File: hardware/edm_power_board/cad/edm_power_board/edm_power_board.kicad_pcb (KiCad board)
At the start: 2 copper layers, 240 x 100 mm, 147 parts, among them J501 Conn_02x08_Odd_Even, J502 Conn_01x02, Q201 SUD19P06-60, Q301 BSS214NW, Q302 BSC13DN30NSFD, Q303 BSS214NW, Q304 BSS214NW, Q601 IPD50R3K0CE, Q602 IPD50R380CE, U201 LM358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

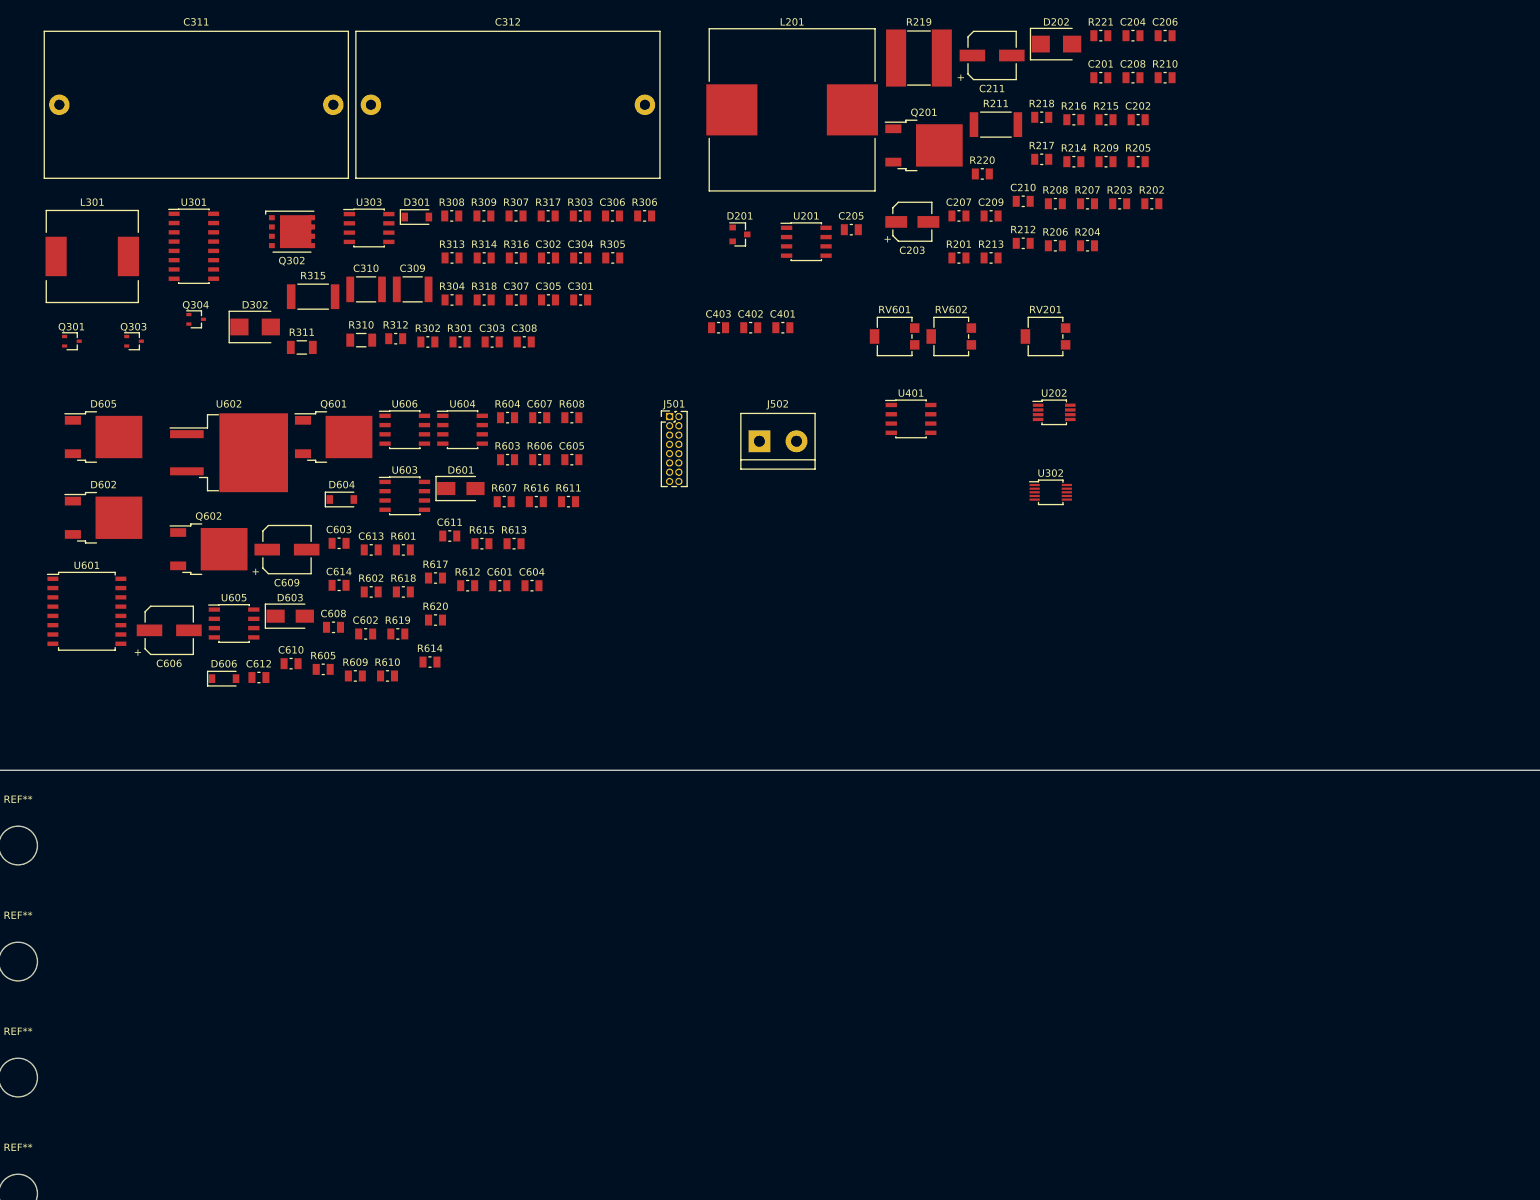
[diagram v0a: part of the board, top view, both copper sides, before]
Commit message: Add input capacitors to spark
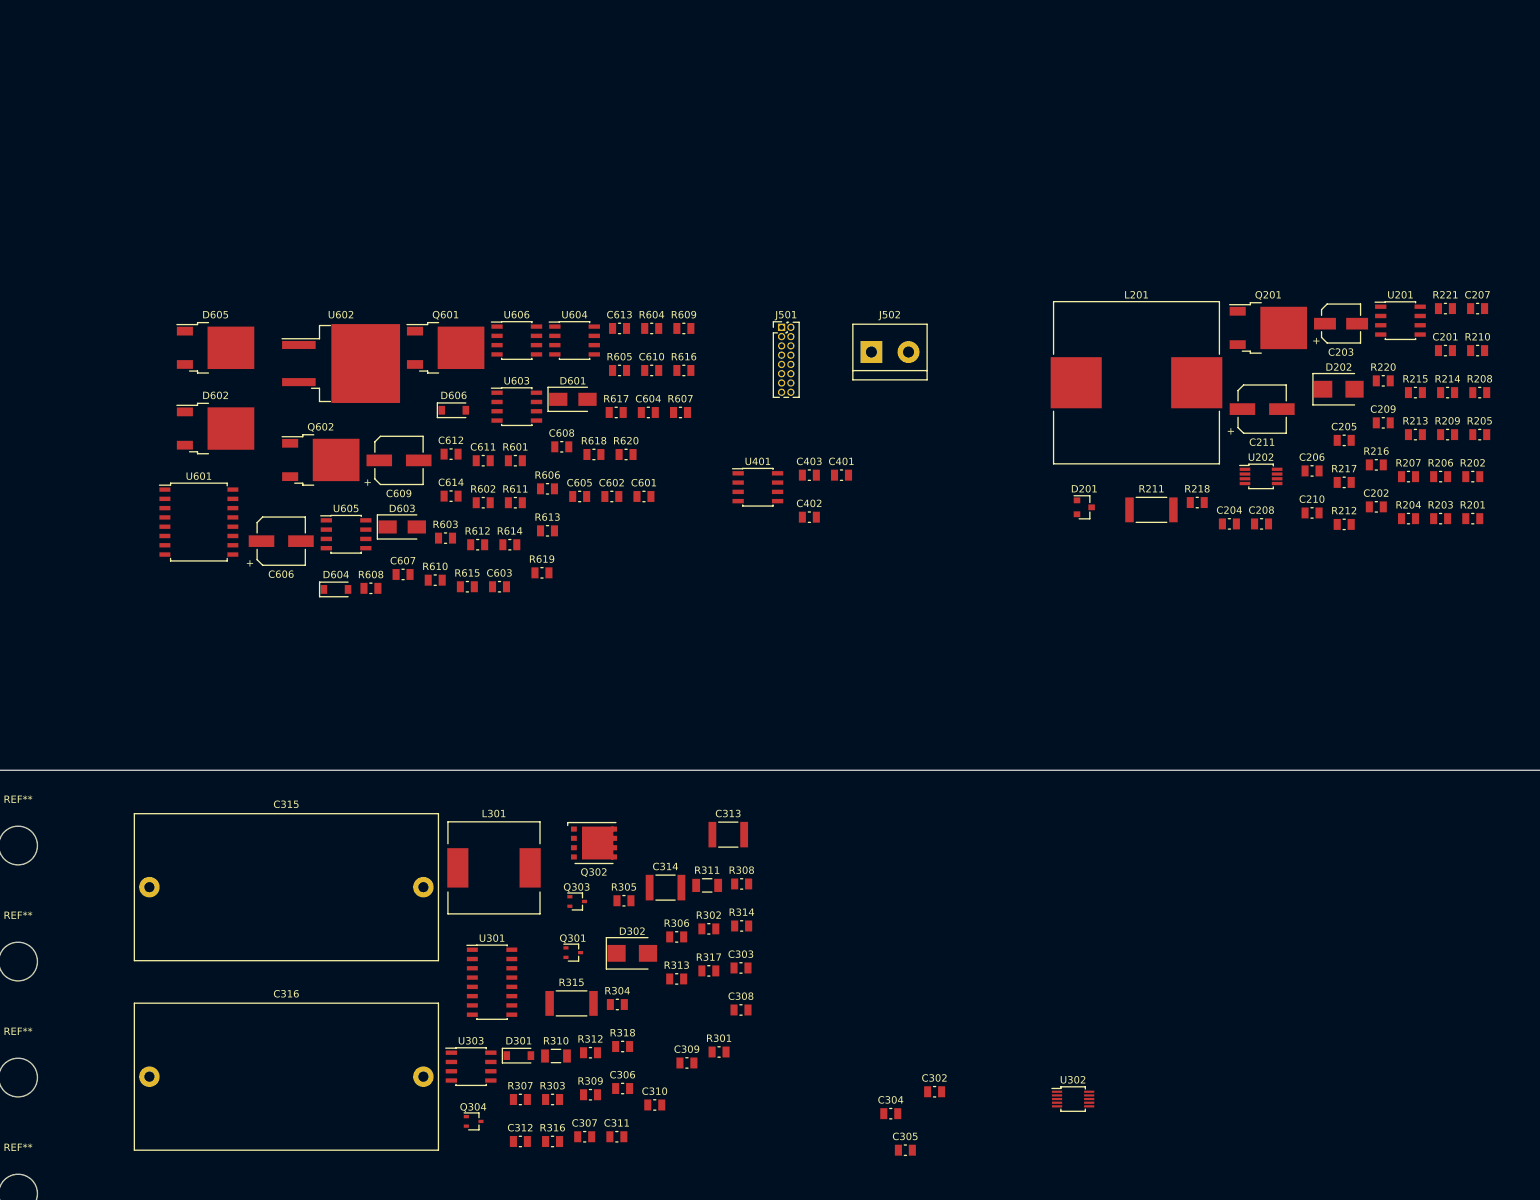
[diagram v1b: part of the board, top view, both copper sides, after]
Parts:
- removed C301: 100n, Capacitor_SMD:C_0805_2012Metric
- removed R219: 20m, Resistor_SMD:R_Stackpole_CSSH2728_4-100m
- removed RV201, RV601: 50k, Potentiometer_SMD:Potentiometer_Bourns_3314G_Horizontal
- removed RV602: 250k, Potentiometer_SMD:Potentiometer_Bourns_3314G_Horizontal
- added C313: 470n, Capacitor_SMD:C_1812_4532Metric, F.Cu at (102.8, -91.2)
- added C314: 470n, Capacitor_SMD:C_1812_4532Metric, F.Cu at (94.2, -83.9)
- added C315: 25u, Capacitor_THT:C_Rect_L41.5mm_W20.0mm_P37.50mm_MKS4, F.Cu at (23.6, -84.0)
- added C316: 25u, Capacitor_THT:C_Rect_L41.5mm_W20.0mm_P37.50mm_MKS4, F.Cu at (23.6, -58.1)
- C302: value 10n -> 1u
- C304: value 100n -> 1u
- C306: value 120n -> 10n
- C307: value 560p -> 100n
- C308: value 1n -> 100n
- C309: value 470n -> 1u; footprint Capacitor_SMD:C_1812_4532Metric -> Capacitor_SMD:C_0805_2012Metric
- C310: value 470n -> 120n; footprint Capacitor_SMD:C_1812_4532Metric -> Capacitor_SMD:C_0805_2012Metric
- C311: value 25u -> 560p; footprint Capacitor_THT:C_Rect_L41.5mm_W20.0mm_P37.50mm_MKS4 -> Capacitor_SMD:C_0805_2012Metric
- C312: value 25u -> 1n; footprint Capacitor_THT:C_Rect_L41.5mm_W20.0mm_P37.50mm_MKS4 -> Capacitor_SMD:C_0805_2012Metric
- moved C311 160.5 mm to (87.6, -49.8)
- moved C312 143.4 mm to (74.4, -49.2)
- moved C305 126.2 mm to (127.0, -48.0)
- moved C302 125.8 mm to (131.0, -56.0)
- moved C304 124.6 mm to (125.0, -53.0)
- moved R309 121.2 mm to (83.9, -55.6)
- moved R316 121.0 mm to (78.8, -49.2)
- moved R303 121.0 mm to (78.8, -54.9)
- moved R307 120.9 mm to (74.4, -54.9)
- moved C306 119.4 mm to (88.3, -56.4)
- moved C310 118.4 mm to (92.7, -54.2)
- moved Q304 116.2 mm to (68.0, -51.9)
- moved D301 115.6 mm to (74.1, -60.9)
- moved U303 115.6 mm to (67.6, -59.4)
- moved C307 114.9 mm to (83.2, -49.8)
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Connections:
- C302 pad 1: Net-(C302-Pad1) -> +24V
- C303 pad 1: +5V -> +3V3
- C303 pad 2: GNDPWR -> GND
- C304 pad 1: +5V -> +24V
- C305 pad 1: Net-(C305-Pad1) -> +24V
- C306 pad 2: Net-(C306-Pad2) -> GNDPWR
- C307 pad 1: Net-(C306-Pad1) -> +5V
- C307 pad 2: Net-(C307-Pad2) -> GNDPWR
- C308 pad 1: Net-(C308-Pad1) -> +5V
- C309 pad 1: /Spark Output/+250V -> Net-(C309-Pad1)
- C310 pad 1: /Spark Output/+250V -> Net-(C310-Pad1)
- C310 pad 2: GNDPWR -> Net-(C310-Pad2)
- C311 pad 1: /Spark Output/+250V -> Net-(C310-Pad1)
- C311 pad 2: GNDPWR -> Net-(C311-Pad2)
- C312 pad 1: /Spark Output/+250V -> Net-(C312-Pad1)
- R305 pad 1: Net-(C306-Pad2) -> Net-(C310-Pad2)
- R305 pad 2: Net-(C307-Pad2) -> Net-(C311-Pad2)
- R308 pad 1: Net-(C306-Pad1) -> Net-(C310-Pad1)
- R309 pad 1: Net-(C308-Pad1) -> Net-(C312-Pad1)
- R313 pad 1: Net-(C306-Pad1) -> Net-(C310-Pad1)
- R314 pad 2: Net-(C308-Pad1) -> Net-(C312-Pad1)
- R316 pad 1: Net-(C306-Pad1) -> Net-(C310-Pad1)
- R317 pad 2: Net-(C306-Pad1) -> Net-(C310-Pad1)
- R318 pad 1: Net-(C306-Pad1) -> Net-(C310-Pad1)
- U302 pad 10: Net-(C302-Pad1) -> Net-(C306-Pad1)
- U302 pad 2: Net-(C306-Pad1) -> Net-(C310-Pad1)
- U302 pad 3: Net-(C307-Pad2) -> Net-(C311-Pad2)
- U302 pad 4: Net-(C305-Pad1) -> Net-(C309-Pad1)

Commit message: Component placement 250V
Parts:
- added C301: 22u, Capacitor_SMD:CP_Elec_5x5.3, F.Cu at (125.2, -42.1)
- added R219: 20m, Resistor_SMD:R_Stackpole_CSSH2728_4-100m, F.Cu at (216.2, -139.1)
- added RV201: 50k, Potentiometer_SMD:Potentiometer_Bourns_3314G_Horizontal, F.Cu at (10.2, -151.8)
- added RV601: 50k, Potentiometer_SMD:Potentiometer_Bourns_3314G_Horizontal, F.Cu at (-10.4, -151.8)
- added RV602: 250k, Potentiometer_SMD:Potentiometer_Bourns_3314G_Horizontal, F.Cu at (-2.67, -151.8)
- moved C316 147.9 mm to (169.6, -81.5)
- moved J501 140.9 mm to (221.1, -73.9)
- moved U301 108.4 mm to (169.2, -26.2), turned to 180 degrees
- moved C315 102.5 mm to (126.0, -81.4)
- moved Q304 96.0 mm to (159.2, -22.2), turned to 180 degrees
- moved Q303 96.0 mm to (159.2, -24.9), turned to 180 degrees
- moved U303 94.5 mm to (160.4, -41.6)
- moved Q301 91.0 mm to (159.2, -27.6), turned to 180 degrees
- moved D301 88.2 mm to (158.7, -35.6)
- moved R304 83.1 mm to (166.0, -40.2), turned to 270 degrees
- moved C307 83.1 mm to (166.0, -43.9), turned to 90 degrees
- moved R310 81.4 mm to (154.8, -30.6)
- moved R308 80.7 mm to (155.6, -21.9)
- moved L301 80.7 mm to (128.6, -30.4), turned to 270 degrees
- moved R307 80.5 mm to (153.5, -40.3), turned to 270 degrees
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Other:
- copper layers 2 -> 4

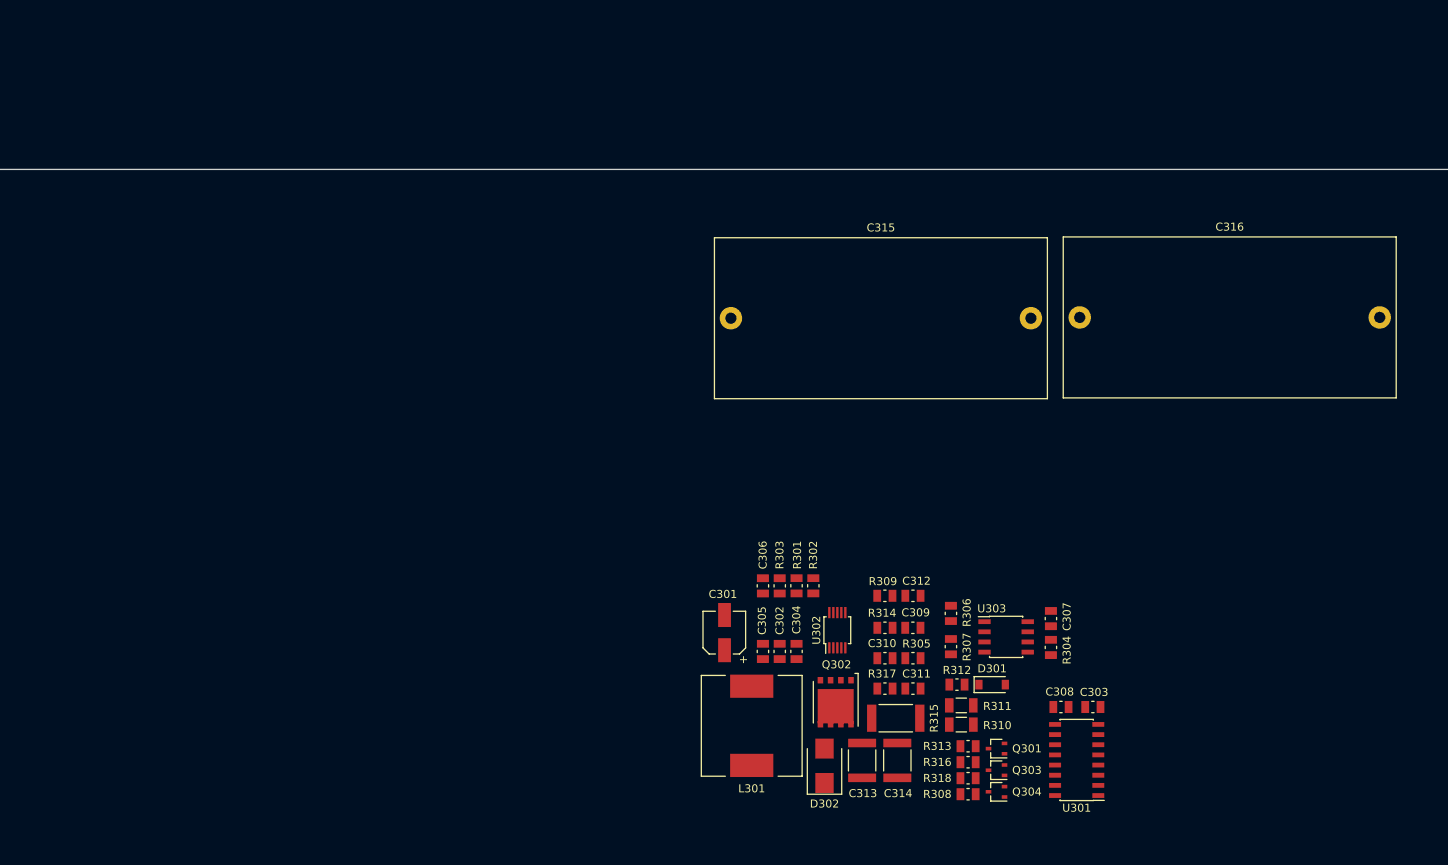
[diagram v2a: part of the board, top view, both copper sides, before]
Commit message: Spark output connector
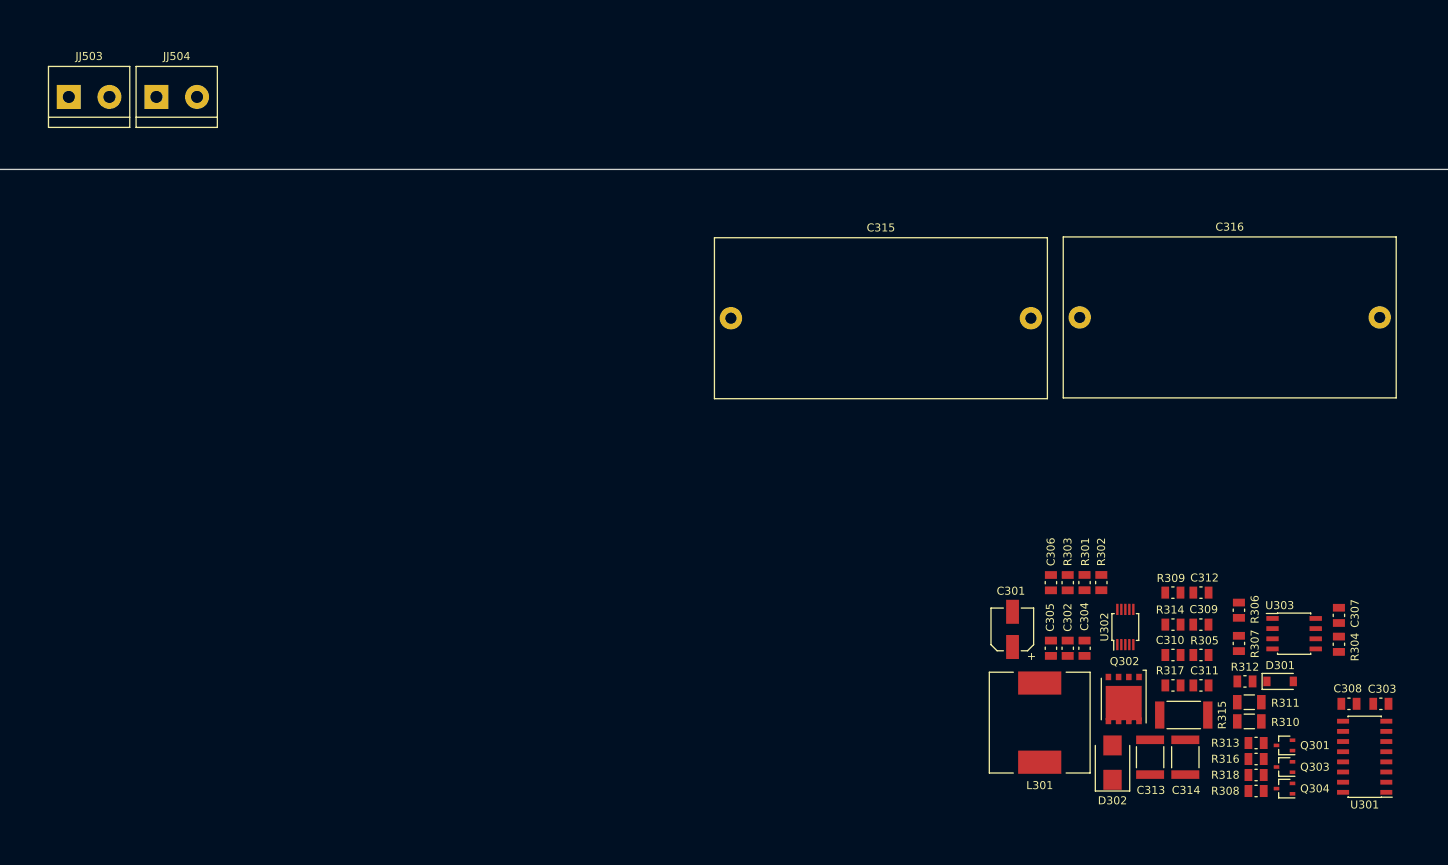
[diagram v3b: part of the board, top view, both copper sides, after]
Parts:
- added JJ503: Conn_01x02, TerminalBlock:TerminalBlock_bornier-2_P5.08mm, F.Cu at (43.2, -109.1)
- added JJ504: Conn_01x02, TerminalBlock:TerminalBlock_bornier-2_P5.08mm, F.Cu at (54.2, -109.1)
- moved C302 36.0 mm to (168.1, -40.1)
- moved C303 36.0 mm to (207.2, -33.2)
- moved C304 36.0 mm to (170.2, -40.1)
- moved C305 36.0 mm to (166.0, -40.1)
- moved C306 36.0 mm to (166.0, -48.3)
- moved C307 36.0 mm to (202.0, -44.3)
- moved C308 36.0 mm to (203.3, -33.2)
- moved C309 36.0 mm to (184.7, -43.1)
- moved C310 36.0 mm to (181.3, -39.3)
- moved C311 36.0 mm to (184.8, -35.5)
- moved C312 36.0 mm to (184.8, -47.1)
- moved C313 36.0 mm to (178.4, -26.5)
- moved C314 36.0 mm to (182.8, -26.5)
- moved D301 36.0 mm to (194.7, -36.0)
- moved D302 36.0 mm to (173.7, -25.9)
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
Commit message: Plated mounting holes
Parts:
- removed REF** (x12): MountingHole_5.3mm_M5, MountingHole:MountingHole_5.3mm_M5
- added MK501: Mounting_Hole_PAD, MountingHole:MountingHole_5mm_Pad, F.Cu at (5.60, -10.3)
- added MK502: Mounting_Hole_PAD, MountingHole:MountingHole_5mm_Pad, F.Cu at (5.60, -26.2)
- added MK503: Mounting_Hole_PAD, MountingHole:MountingHole_5mm_Pad, F.Cu at (5.60, -42.1)
- added MK504: Mounting_Hole_PAD, MountingHole:MountingHole_5mm_Pad, F.Cu at (5.60, -57.9)
- added MK505: Mounting_Hole_PAD, MountingHole:MountingHole_5mm_Pad, F.Cu at (5.60, -73.8)
- added MK506: Mounting_Hole_PAD, MountingHole:MountingHole_5mm_Pad, F.Cu at (5.60, -89.7)
- added MK507: Mounting_Hole_PAD, MountingHole:MountingHole_5mm_Pad, F.Cu at (234.4, -10.3)
- added MK508: Mounting_Hole_PAD, MountingHole:MountingHole_5mm_Pad, F.Cu at (234.4, -26.2)
- added MK509: Mounting_Hole_PAD, MountingHole:MountingHole_5mm_Pad, F.Cu at (234.4, -42.1)
- added MK510: Mounting_Hole_PAD, MountingHole:MountingHole_5mm_Pad, F.Cu at (234.4, -57.9)
- added MK511: Mounting_Hole_PAD, MountingHole:MountingHole_5mm_Pad, F.Cu at (234.4, -73.8)
- added MK512: Mounting_Hole_PAD, MountingHole:MountingHole_5mm_Pad, F.Cu at (234.4, -89.7)
- U301: value Si8641BB-B-IS1 -> Si8641BB-B-IS; footprint Package_SO:SOIC-16_3.9x9.9mm_P1.27mm -> Package_SO:SOIC-16W_7.5x10.3mm_P1.27mm
- moved R214 180.0 mm to (58.5, -42.1), turned to 270 degrees
- moved C207 178.7 mm to (69.3, -47.4), turned to 270 degrees
- moved R210 178.3 mm to (65.1, -47.4), turned to 270 degrees
- moved C209 172.2 mm to (56.4, -42.0), turned to 90 degrees
- moved R213 171.3 mm to (60.6, -42.1), turned to 90 degrees
- moved D202 171.3 mm to (71.3, -25.2)
- moved R209 171.3 mm to (68.7, -37.4), turned to 90 degrees
- moved R205 170.0 mm to (67.2, -47.4), turned to 270 degrees
- moved C211 165.7 mm to (47.2, -45.1), turned to 90 degrees
- moved Q201 165.5 mm to (73.2, -31.4)
- moved L201 162.8 mm to (55.6, -27.1), turned to 90 degrees
- moved C203 161.6 mm to (75.6, -43.7), turned to 90 degrees
- moved R212 161.3 mm to (54.3, -42.0), turned to 270 degrees
- moved C210 160.4 mm to (52.2, -42.0), turned to 90 degrees
- moved U202 147.3 mm to (65.8, -42.1)
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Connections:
- net Net-(C201-Pad1) renamed /Current Source/CS_2-
- net Net-(C205-Pad1) renamed /Current Source/CS_1
- net Net-(C205-Pad2) renamed /Current Source/CS_2+
- net Net-(C206-Pad1) renamed /Current Source/CS_3
- net Net-(C206-Pad2) renamed /Current Source/CS_2
- net Net-(C207-Pad2) renamed /Current Source/CS_VCC
- net Net-(C208-Pad2) renamed /Current Source/CS_ADJ
- net Net-(C209-Pad1) renamed /Current Source/CS_QD1
- net Net-(C210-Pad1) renamed /Current Source/CS_OUT
- net Net-(D201-Pad1) renamed /Current Source/CS_4
- net Net-(D202-Pad1) renamed /Current Source/CS_QD
- net Net-(Q201-Pad1) renamed /Current Source/CS_PGATE
- net Net-(Q201-Pad3) renamed /Current Source/CS_QS
- net Net-(R202-Pad2) renamed /Current Source/CS_NC1
- net Net-(R205-Pad2) renamed /Current Source/CS_RT
- net Net-(R209-Pad2) renamed /Current Source/CS_ISEN
- net Net-(R215-Pad1) renamed /Current Source/CS_1-
- net Net-(R216-Pad1) renamed /Current Source/CS_1+
- net Net-(U201-Pad1) renamed /Current Source/CS_NC2
- C209 pad 2: Net-(C209-Pad2) -> /Current Source/CS_FB
- C211 pad 2: GND -> GNDPWR
- R204 pad 1: Net-(R204-Pad1) -> /Current Source/CS_FB
- R213 pad 2: Net-(C209-Pad2) -> /Current Source/CS_FB
- R214 pad 1: Net-(C209-Pad2) -> /Current Source/CS_FB
- RV201 pad 2: Net-(R204-Pad1) -> /Current Source/CS_FB
- U202 pad 3: Net-(C209-Pad2) -> /Current Source/CS_FB
